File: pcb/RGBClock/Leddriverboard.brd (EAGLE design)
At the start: 70 x 47.5 mm, 37 parts, among them U1 LP3878MR-ADJ, U2 P82B96DR, U3 PCA9685PW, U4 ZXLD1362ET5TA, U5 ZXLD1362ET5TA, U6 ZXLD1362ET5TA, X1 43045-0400, X2 43045-0600

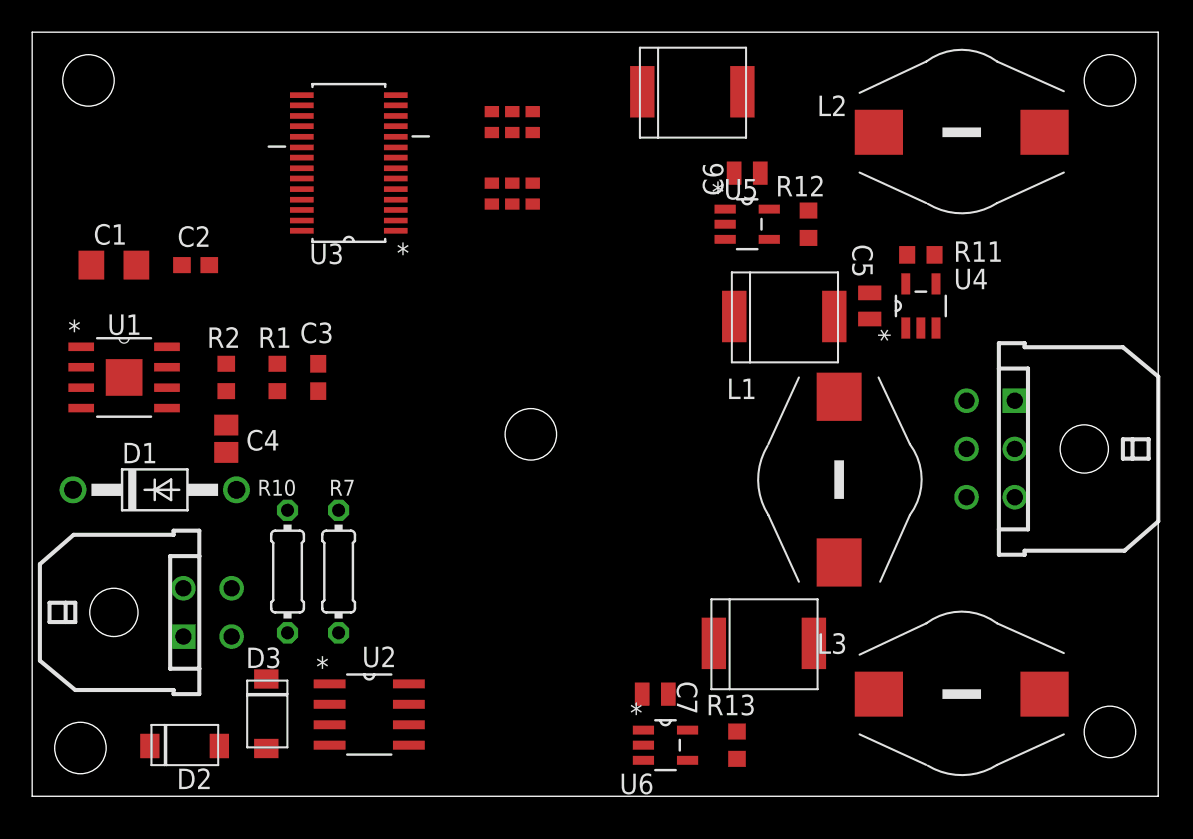
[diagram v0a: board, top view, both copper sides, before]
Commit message: Leddriver board complete
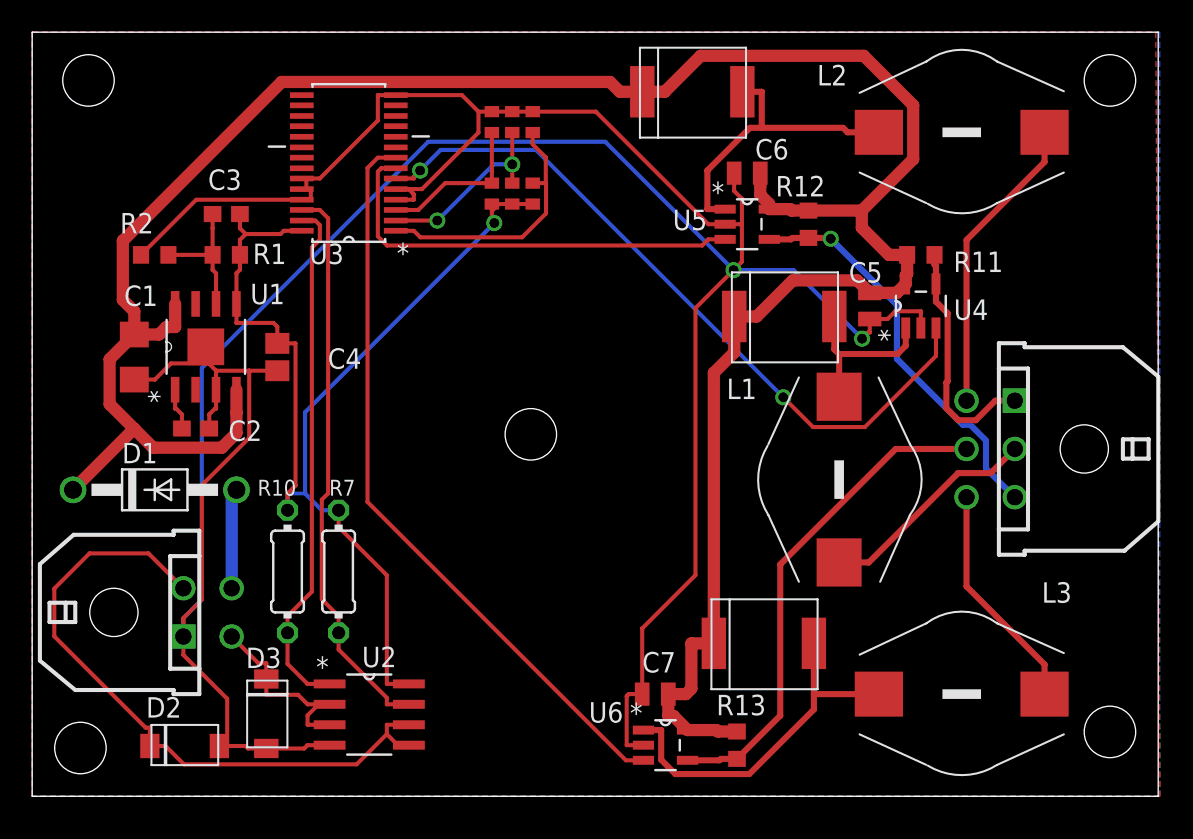
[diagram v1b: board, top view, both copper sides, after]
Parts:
- moved C3 11.7 mm to (12.1, 36.2), turned to 180 degrees
- moved C2 10.2 mm to (10.2, 22.9)
- moved R2 8.82 mm to (7.62, 33.7), turned to 180 degrees
- moved R1 8.26 mm to (12.1, 33.7), turned to 180 degrees
- moved C4 5.99 mm to (15.2, 27.3)
- moved C1 5.85 mm to (6.35, 27.3), turned to 270 degrees
- moved U1 5.43 mm to (10.8, 27.9), turned to 90 degrees
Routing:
- net GND: track 0.00 -> 220.2 mm, vias 0 -> 2
- net VCC: track 0.00 -> 155.7 mm
- net +5V: track 0.00 -> 69.8 mm, vias 0 -> 1
- net N$15: track 0.00 -> 46.6 mm
- net N$8: track 0.00 -> 45.1 mm, vias 0 -> 2
- net N$22: track 0.00 -> 41.8 mm
- net SCL: track 0.00 -> 35.3 mm
- net SDA: track 0.00 -> 32.5 mm
- net N$16: track 0.00 -> 30.9 mm
- net N$2: track 0.00 -> 27.2 mm
- net N$4: track 0.00 -> 25.0 mm, vias 0 -> 1
- net N$19: track 0.00 -> 22.6 mm
- net N$9: track 0.00 -> 18.8 mm
- net N$5: track 0.00 -> 18.7 mm
- net N$41: track 0.00 -> 16.3 mm
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- added copper zone on layer 1, net GND
- added copper zone on layer 16, net GND
